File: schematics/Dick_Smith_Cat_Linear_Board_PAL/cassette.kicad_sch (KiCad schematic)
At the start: 20 parts, among them Q6 1402D, U49 uA741C

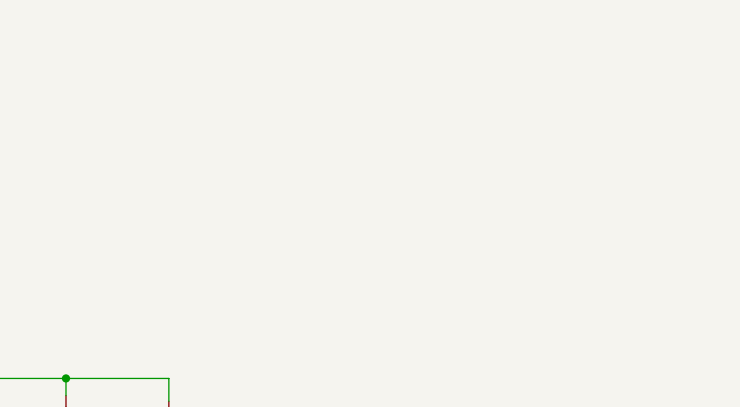
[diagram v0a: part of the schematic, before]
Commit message: Add more connector pinouts to the schematics
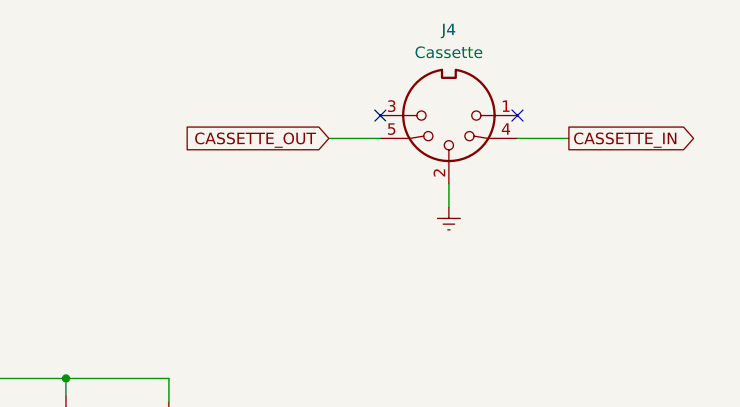
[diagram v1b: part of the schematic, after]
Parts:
- added J4: Cassette, symbol Connector:DIN-5_180degree
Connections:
- net CASSETTE_IN: now also J4.4
- net CASSETTE_OUT: now also J4.5
- net Earth: now also J4.2
- no-connect marks 2 -> 4
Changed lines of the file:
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@@
   (junction (at 166.37 78.105) (diameter 0) (color 0 0 0 0)
   )
+  (no_connect (at 212.09 48.895))
+  (no_connect (at 227.33 48.895))
   (no_connect (at 146.685 111.125))
   (no_connect (at 149.225 111.125))
@@
     (stroke (width 0) (type default))
   )
+  (wire (pts (xy 219.71 56.515) (xy 219.71 59.055))
+    (stroke (width 0) (type default))
+  )
   (wire (pts (xy 115.57 48.895) (xy 125.73 48.895))
     (stroke (width 0) (type default))
@@
     (stroke (width 0) (type default))
   )
+  (wire (pts (xy 206.375 51.435) (xy 212.09 51.435))
+    (stroke (width 0) (type default))
+  )
   (wire (pts (xy 163.195 89.535) (xy 166.37 89.535))
     (stroke (width 0) (type default))
@@
   )
   (wire (pts (xy 156.845 100.965) (xy 166.37 100.965))
+    (stroke (width 0) (type default))
+  )
+  (wire (pts (xy 227.33 51.435) (xy 233.045 51.435))
     (stroke (width 0) (type default))
   )
@@
     )
   )
+  (global_label "CASSETTE_IN" (shape output) (at 233.045 51.435 0) (fields_autoplaced)
+    (effects (font (size 1.27 1.27)) (justify left))
+    (property "Intersheetrefs" "${INTERSHEET_REFS}" (at 247.9439 51.435 0)
+      (effects (font (size 1.27 1.27)) (justify left) hide)
+    )
+  )
   (global_label "CASOUT" (shape input) (at 86.995 48.895 180) (fields_autoplaced)
     (effects (font (size 1.27 1.27)) (justify right))
@@
     )
   )
+  (global_label "CASSETTE_OUT" (shape input) (at 206.375 51.435 180) (fields_autoplaced)
+    (effects (font (size 1.27 1.27)) (justify right))
+    (property "Intersheetrefs" "${INTERSHEET_REFS}" (at 189.7828 51.435 0)
+      (effects (font (size 1.27 1.27)) (justify right) hide)
+    )
+  )
   (global_label "CASSETTE_IN" (shape input) (at 210.82 106.045 0) (fields_autoplaced)
     (effects (font (size 1.27 1.27)) (justify left))
@@
     )
   )
+  (symbol (lib_id "Connector:DIN-5_180degree") (at 219.71 48.895 180) (unit 1)
+    (in_bom yes) (on_board yes) (dnp no) (fields_autoplaced)
+    (property "Reference" "J4" (at 219.7099 39.37 0)
+      (effects (font (size 1.27 1.27)))
+    )
+    (property "Value" "Cassette" (at 219.7099 41.91 0)
+      (effects (font (size 1.27 1.27)))
+    )
+    (property "Footprint" "" (at 219.71 48.895 0)
+      (effects (font (size 1.27 1.27)) hide)
+    )
+    (property "Datasheet" "http://www.mouser.com/ds/2/18/40_c091_abd_e-75918.pdf" (at 219.71 48.895 0)
+      (effects (font (size 1.27 1.27)) hide)
+    )
+    (pin "1")
+    (pin "5")
+    (pin "3")
+    (pin "2")
+    (pin "4")
+    (instances
+      (project "Dick_Smith_Cat_Linear_Board_PAL"
+        (path "/cc76f27d-e855-48d8-b206-3df41b400bec/6fedbba3-b298-40c5-9a22-9fd3d6c59715"
+          (reference "J4") (unit 1)
+        )
+      )
+    )
+  )
   (symbol (lib_id "Device:R_US") (at 102.235 83.82 0) (unit 1)
     (in_bom yes) (on_board yes) (dnp no) (fields_autoplaced)
@@
         )
       )
+    )
+  )
+  (symbol (lib_id "power:Earth") (at 219.71 59.055 0) (unit 1)
+    (in_bom yes) (on_board yes) (dnp no) (fields_autoplaced)
+    (property "Reference" "#PWR049" (at 219.71 65.405 0)
+      (effects (font (size 1.27 1.27)) hide)
+    )
+    (property "Value" "Earth" (at 219.71 62.865 0)
+      (effects (font (size 1.27 1.27)) hide)
+    )
+    (property "Footprint" "" (at 219.71 59.055 0)
+      (effects (font (size 1.27 1.27)) hide)
+    )
+    (property "Datasheet" "~" (at 219.71 59.055 0)
+      (effects (font (size 1.27 1.27)) hide)
+    )
+    (pin "1")
+    (instances
+      (project "Dick_Smith_Cat_Linear_Board_PAL"
+        (path "/cc76f27d-e855-48d8-b206-3df41b400bec/6fedbba3-b298-40c5-9a22-9fd3d6c59715"
+          (reference "#PWR049") (unit 1)
+        )
+      )
